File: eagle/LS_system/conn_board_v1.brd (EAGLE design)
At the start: 47 x 31.8 mm, 11 parts, among them X7 MURDOCK_STACK

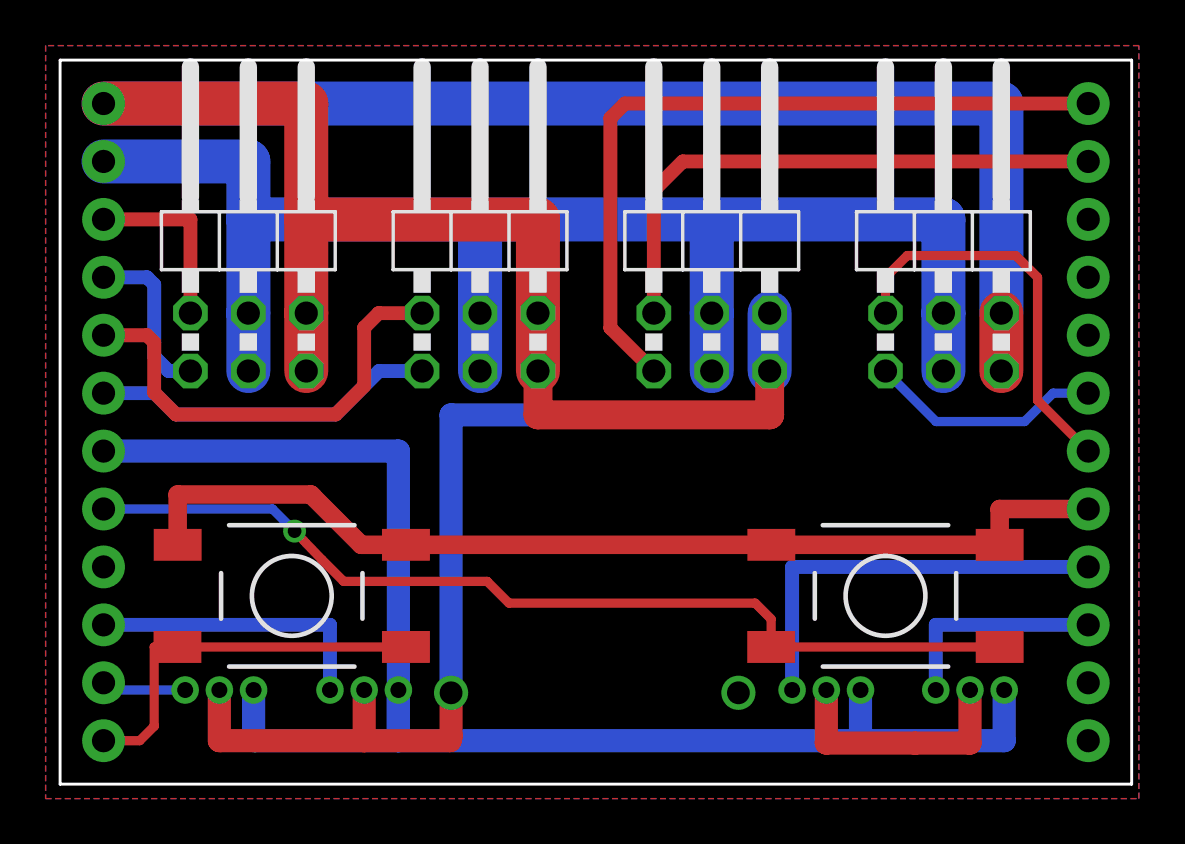
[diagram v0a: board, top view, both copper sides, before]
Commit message: mirrored spektrum & moved buttons
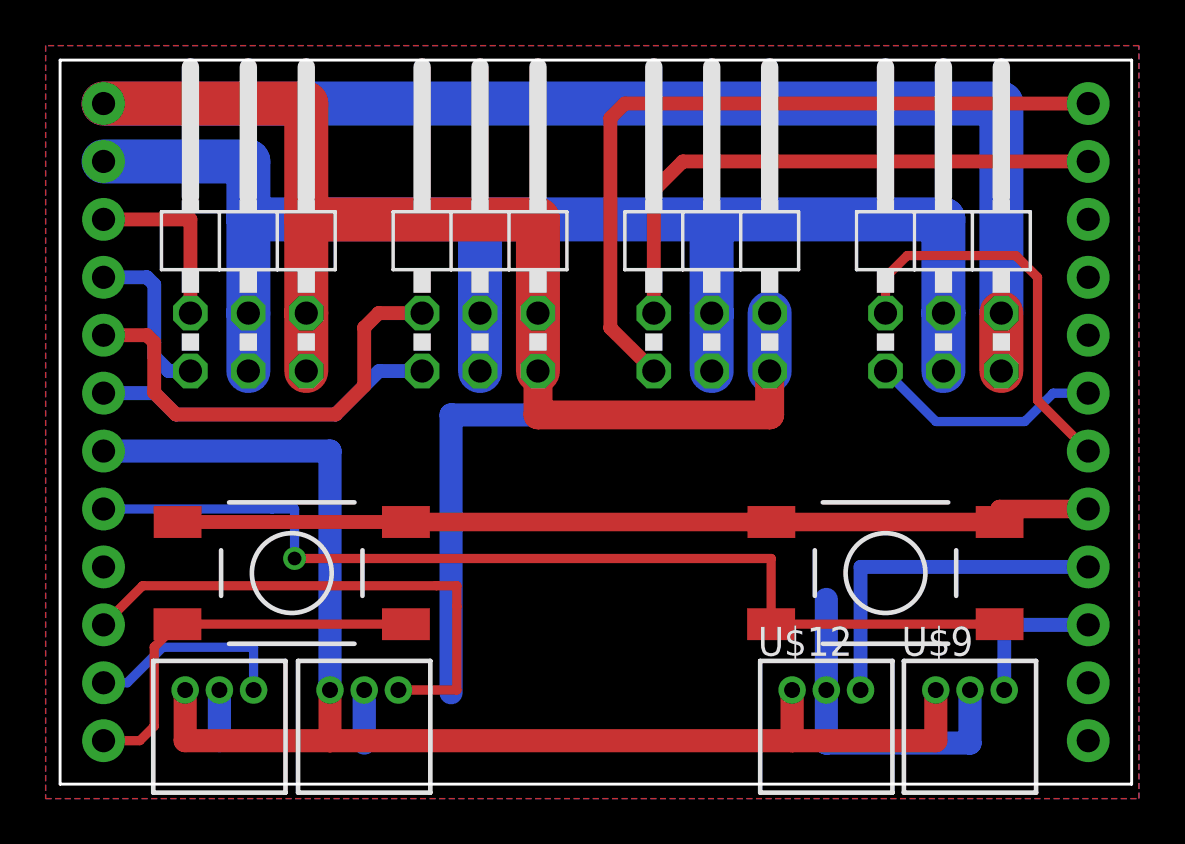
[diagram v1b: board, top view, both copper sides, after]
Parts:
- moved S1 1.00 mm to (10.2, 9.26)
- moved S2 1.00 mm to (36.2, 9.26)
- flipped U$10 to the top
- flipped U$11 to the top
- flipped U$12 to the top
- flipped U$9 to the top
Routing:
- net SP2: track 12.8 -> 23.3 mm
- net GND: track 150.6 -> 142.5 mm, vias 2 -> 0
- net SP1: track 3.71 -> 9.10 mm
- net 3V3SP: track 67.4 -> 62.2 mm
- net 3.3V: track 44.6 -> 40.5 mm
- net TX: track 18.4 -> 15.4 mm
- net RX: track 9.54 -> 6.54 mm
- net SW2: track 42.5 -> 44.3 mm

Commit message: switch part-numbers
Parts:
- S1, S2: value (none) -> min: "taster 9318" max: "taster 9319"
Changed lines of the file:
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@@
 <element name="U$10" library="seb" package="S3B-ZR" value="S3B-ZR" x="6.985" y="4.1275" smashed="yes"/>
 <element name="U$11" library="seb" package="S3B-ZR" value="S3B-ZR" x="13.335" y="4.1275" smashed="yes"/>
-<element name="S2" library="switch-tact" package="LSH" value="" x="36.195" y="9.255" smashed="yes" rot="R180">
+<element name="S2" library="switch-tact" package="LSH" value="min: &quot;taster 9318&quot; max: &quot;taster 9319&quot;" x="36.195" y="9.255" smashed="yes" rot="R180">
 <attribute name="VALUE" x="38.735" y="14.335" size="1.27" layer="27" rot="R180"/>
 </element>
-<element name="S1" library="switch-tact" package="LSH" value="" x="10.16" y="9.255" smashed="yes" rot="R180">
+<element name="S1" library="switch-tact" package="LSH" value="min: &quot;taster 9318&quot; max: &quot;taster 9319&quot;" x="10.16" y="9.255" smashed="yes" rot="R180">
 <attribute name="VALUE" x="12.7" y="14.335" size="1.27" layer="27" rot="R180"/>
 </element>
